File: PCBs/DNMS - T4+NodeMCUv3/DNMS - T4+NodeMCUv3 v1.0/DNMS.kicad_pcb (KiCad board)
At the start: 2 copper layers, 60 x 32.5 mm, 23 parts, among them J1 Conn_01x06, J2 Conn_01x02, J3 Conn_01x04, J4 Conn_01x05, J5 Conn_01x06, J6 Conn_01x05, U2 NodeMCU V3, U3 Teensy4.0

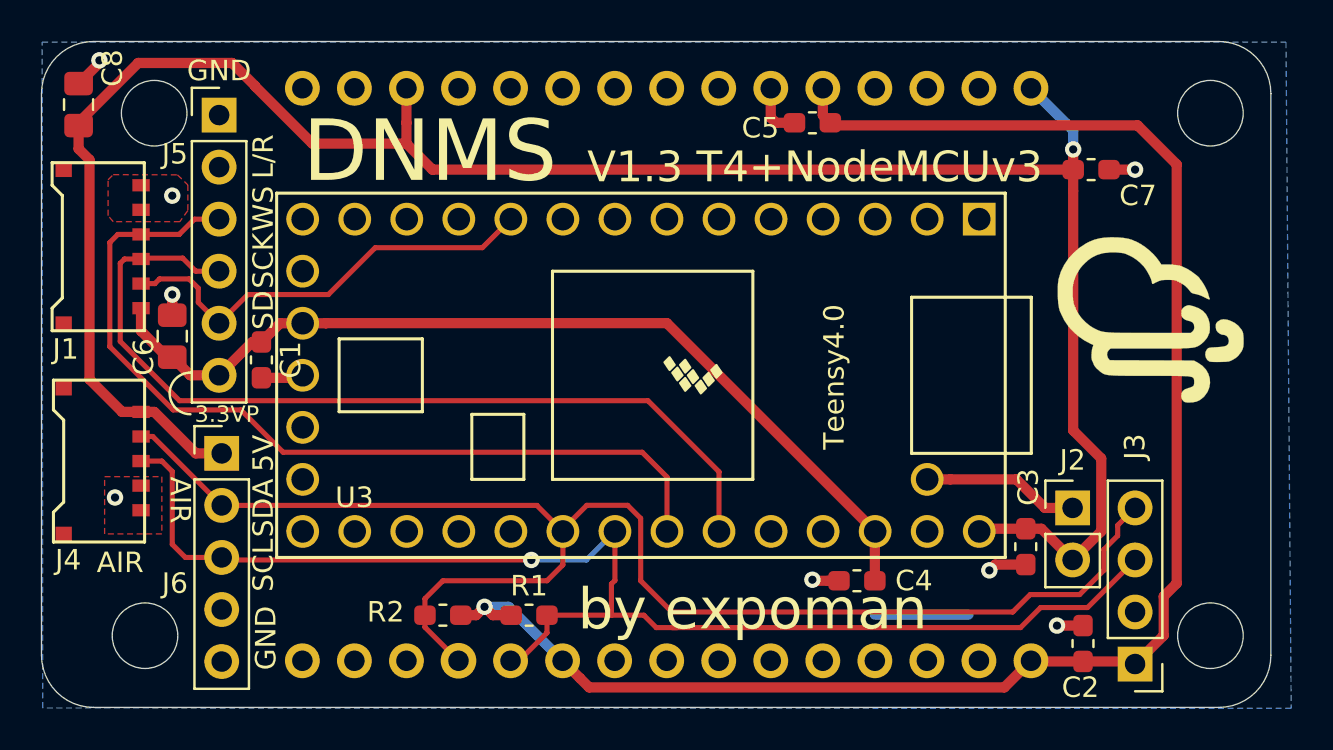
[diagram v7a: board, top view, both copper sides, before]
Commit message: optimize few text labels
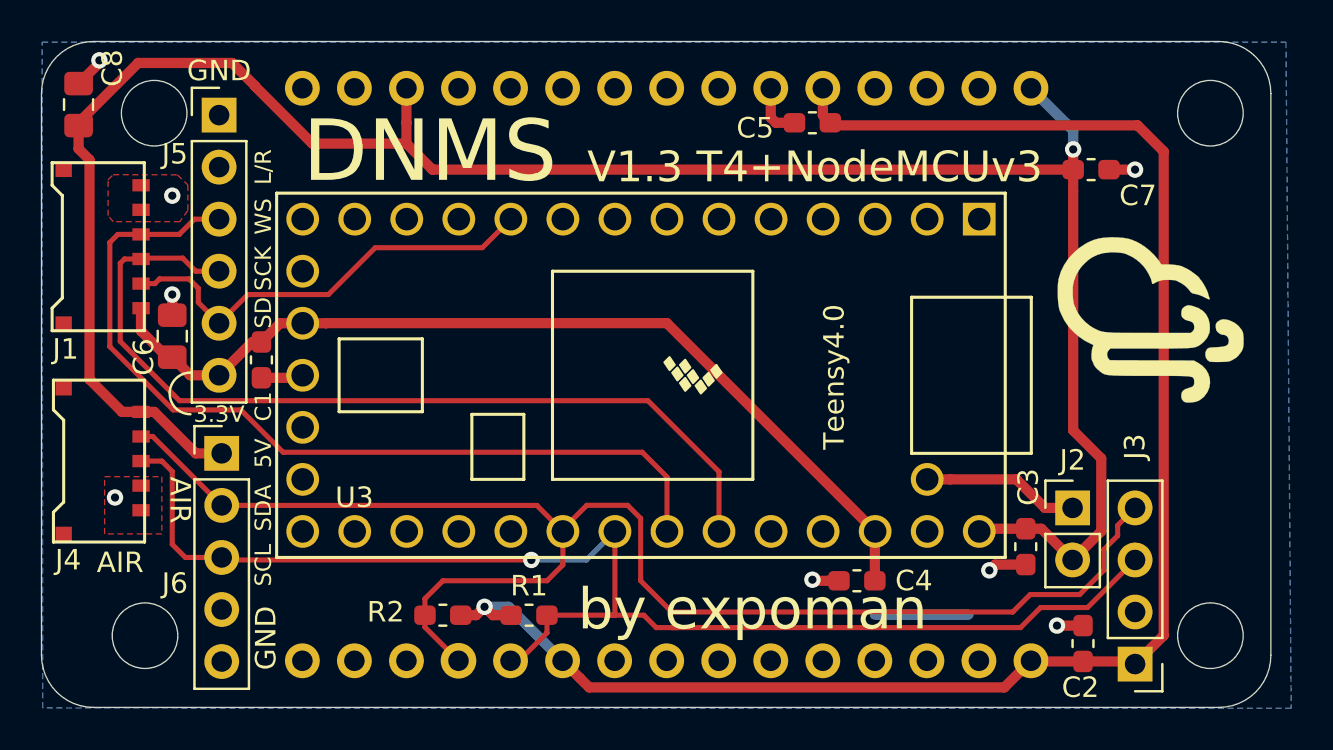
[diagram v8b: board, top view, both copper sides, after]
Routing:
- net +3V3: track 82.0 -> 81.5 mm
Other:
- board text added: "3.3V"
- board text removed: "3.3VP"
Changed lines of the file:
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@@
     (thickness 1.6)
     (drawings 24)
-    (tracks 198)
+    (tracks 196)
     (zones 0)
     (modules 23)
@@
   )
   (setup
-    (last_trace_width 0.5)
+    (last_trace_width 0.25)
     (user_trace_width 0.5)
     (trace_clearance 0.2)
@@
     (tags "capacitor handsolder")
     (attr smd)
-    (fp_text reference C5 (at 2.54 -0.254) (layer F.SilkS)
+    (fp_text reference C5 (at 2.794 -0.254) (layer F.SilkS)
       (effects (font (size 1 1) (thickness 0.15)))
     )
@@
     (tags "capacitor handsolder")
     (attr smd)
-    (fp_text reference C1 (at 0 -1.43 90) (layer F.SilkS)
-      (effects (font (size 1 1) (thickness 0.15)))
+    (fp_text reference C1 (at 2.272 -0.093 90) (layer F.SilkS)
+      (effects (font (size 0.8 0.8) (thickness 0.15)))
     )
     (fp_text value 100nF (at 0 1.43 90) (layer F.Fab)
@@
   )
   (gr_text SCL (at 76.327 83.058 90) (layer F.SilkS)
-    (effects (font (size 1 1) (thickness 0.15)))
+    (effects (font (size 0.8 0.8) (thickness 0.15)))
   )
   (gr_text SDA (at 76.327 80.264 90) (layer F.SilkS)
-    (effects (font (size 1 1) (thickness 0.15)))
+    (effects (font (size 0.8 0.8) (thickness 0.15)))
   )
   (gr_text 5V (at 76.327 77.597 90) (layer F.SilkS)
-    (effects (font (size 1 1) (thickness 0.15)))
+    (effects (font (size 0.8 0.8) (thickness 0.15)))
   )
   (gr_arc (start 72.771 74.676) (end 72.771 73.66) (angle -180) (layer F.SilkS) (width 0.12))
@@
     (effects (font (size 3 3) (thickness 0.75)))
   )
-  (gr_text SD (at 76.327 70.612 90) (layer F.SilkS)
-    (effects (font (size 1 1) (thickness 0.15)))
-  )
-  (gr_text "WS\n" (at 76.327 65.659 90) (layer F.SilkS)
-    (effects (font (size 1 1) (thickness 0.15)))
-  )
-  (gr_text 3.3VP (at 74.549 75.692) (layer F.SilkS)
+  (gr_text SD (at 76.327 70.739 90) (layer F.SilkS)
     (effects (font (size 0.8 0.8) (thickness 0.15)))
   )
-  (gr_text SCK (at 76.327 68.199 90) (layer F.SilkS)
-    (effects (font (size 1 1) (thickness 0.15)))
-  )
-  (gr_text L/R (at 76.327 63.119 90) (layer F.SilkS)
-    (effects (font (size 1 1) (thickness 0.15)))
+  (gr_text "WS\n" (at 76.327 66.04 90) (layer F.SilkS)
+    (effects (font (size 0.8 0.8) (thickness 0.15)))
+  )
+  (gr_text 3.3V (at 74.168 75.692) (layer F.SilkS)
+    (effects (font (size 0.8 0.8) (thickness 0.15)))
+  )
+  (gr_text SCK (at 76.327 68.58 90) (layer F.SilkS)
+    (effects (font (size 0.8 0.8) (thickness 0.15)))
+  )
+  (gr_text L/R (at 76.327 63.627 90) (layer F.SilkS)
+    (effects (font (size 0.8 0.8) (thickness 0.15)))
   )
   (gr_text GND (at 74.168 58.928) (layer F.SilkS)
@@
   (segment (start 116.332 87.757) (end 118.745 87.757) (width 0.5) (layer F.Cu) (net 2))
   (segment (start 119.0244 87.7316) (end 118.872 87.884) (width 0.5) (layer F.Cu) (net 2))
+  (segment (start 120.269 86.487) (end 120.269 62.865) (width 0.5) (layer F.Cu) (net 2))
+  (segment (start 118.872 87.884) (end 120.269 86.487) (width 0.5) (layer F.Cu) (net 2))
+  (segment (start 120.269 62.865) (end 118.999 61.595) (width 0.5) (layer F.Cu) (net 2))
   (segment (start 104.113939 61.468) (end 103.999 61.468) (width 0.5) (layer F.Cu) (net 2))
+  (segment (start 118.999 61.595) (end 104.240939 61.595) (width 0.5) (layer F.Cu) (net 2))
   (segment (start 104.240939 61.595) (end 104.113939 61.468) (width 0.5) (layer F.Cu) (net 2))
-  (segment (start 118.999 61.595) (end 104.240939 61.595) (width 0.5) (layer F.Cu) (net 2))
-  (segment (start 120.269 86.487) (end 120.269 84.582) (width 0.5) (layer F.Cu) (net 2))
-  (segment (start 118.872 87.884) (end 120.269 86.487) (width 0.5) (layer F.Cu) (net 2))
-  (segment (start 120.269 84.582) (end 120.904 83.947) (width 0.5) (layer F.Cu) (net 2))
-  (segment (start 120.904 83.947) (end 120.904 63.5) (width 0.5) (layer F.Cu) (net 2))
-  (segment (start 120.904 63.5) (end 118.999 61.595) (width 0.5) (layer F.Cu) (net 2))
   (segment (start 83.312 59.78398) (end 83.312 61.468) (width 0.5) (layer F.Cu) (net 3))
   (segment (start 83.312 61.468) (end 83.312 62.484) (width 0.5) (layer F.Cu) (net 3))
@@
   (segment (start 94.107 80.137) (end 92.113 80.137) (width 0.25) (layer F.Cu) (net 4))
   (segment (start 94.742 83.82) (end 94.742 80.772) (width 0.25) (layer F.Cu) (net 4))
-  (segment (start 93.48724 81.4115) (end 93.48724 83.80476) (width 0.25) (layer F.Cu) (net 5))
   (segment (start 93.48724 81.4115) (end 93.48724 81.04124) (width 0.25) (layer B.Cu) (net 5))
   (via (at 89.408 82.804) (size 0.8) (drill 0.4) (layers F.Cu B.Cu) (net 5))
@@
   (segment (start 95.504 86.106) (end 96.52 86.106) (width 0.25) (layer F.Cu) (net 5))
   (segment (start 94.898 85.5) (end 95.504 86.106) (width 0.25) (layer F.Cu) (net 5))
-  (segment (start 93.316 85.5) (end 93.316 83.976) (width 0.25) (layer F.Cu) (net 5))
-  (segment (start 93.316 85.5) (end 94.898 85.5) (width 0.25) (layer F.Cu) (net 5))
-  (segment (start 93.316 83.976) (end 93.48724 83.80476) (width 0.25) (layer F.Cu) (net 5))
   (segment (start 90.17 85.5) (end 93.316 85.5) (width 0.25) (layer F.Cu) (net 5))
+  (segment (start 93.48724 85.48624) (end 93.48724 81.4115) (width 0.25) (layer F.Cu) (net 5))
+  (segment (start 93.501 85.5) (end 93.48724 85.48624) (width 0.25) (layer F.Cu) (net 5))
+  (segment (start 93.501 85.5) (end 94.898 85.5) (width 0.25) (layer F.Cu) (net 5))
+  (segment (start 93.316 85.5) (end 93.501 85.5) (width 0.25) (layer F.Cu) (net 5))
   (segment (start 73.152 70.2355) (end 74.168 71.2515) (width 0.25) (layer F.Cu) (net 6))
   (segment (start 71.033 69.316) (end 71.261 69.088) (width 0.25) (layer F.Cu) (net 6))
